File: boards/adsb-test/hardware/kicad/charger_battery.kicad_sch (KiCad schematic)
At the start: 0 parts

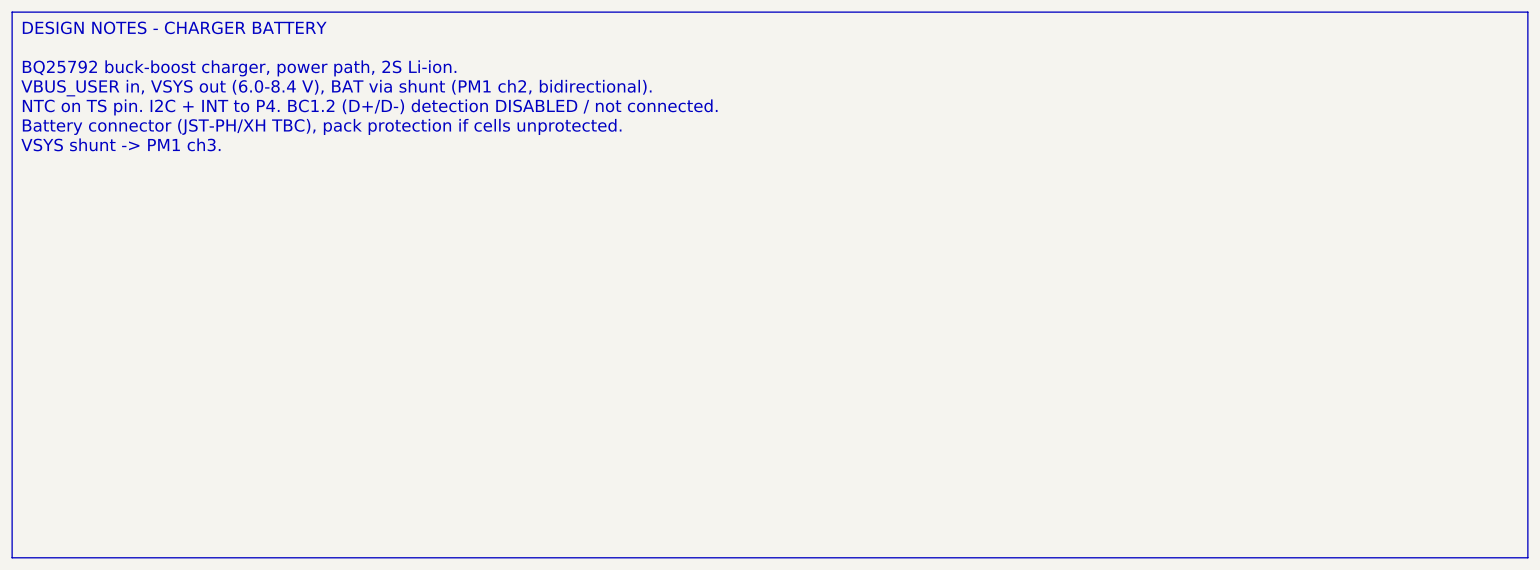
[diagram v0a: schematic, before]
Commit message: Release v0.4.0: ADSB_Test with ESP32-C5, ADSBee m1421 and LA5016 header
- C6 -> C5 co-processor; m1421 identified and integrated (symbol/footprint
  from the ADSBee 1421 carrier, GPL-3.0 attribution)
- Power budget and 2S1P battery sizing for >= 1 h; USB-A for 1-2 SDRs via hub
- Dev port: FT2232H + RP2040 debugprobe; TCA6408A expander for slow I/O
- Test Debug sheet with LA5016 header and rail test points
- Vendor documents git-ignored (public repo)

Co-Authored-By: Claude Opus 5.5 <noreply@anthropic.com>
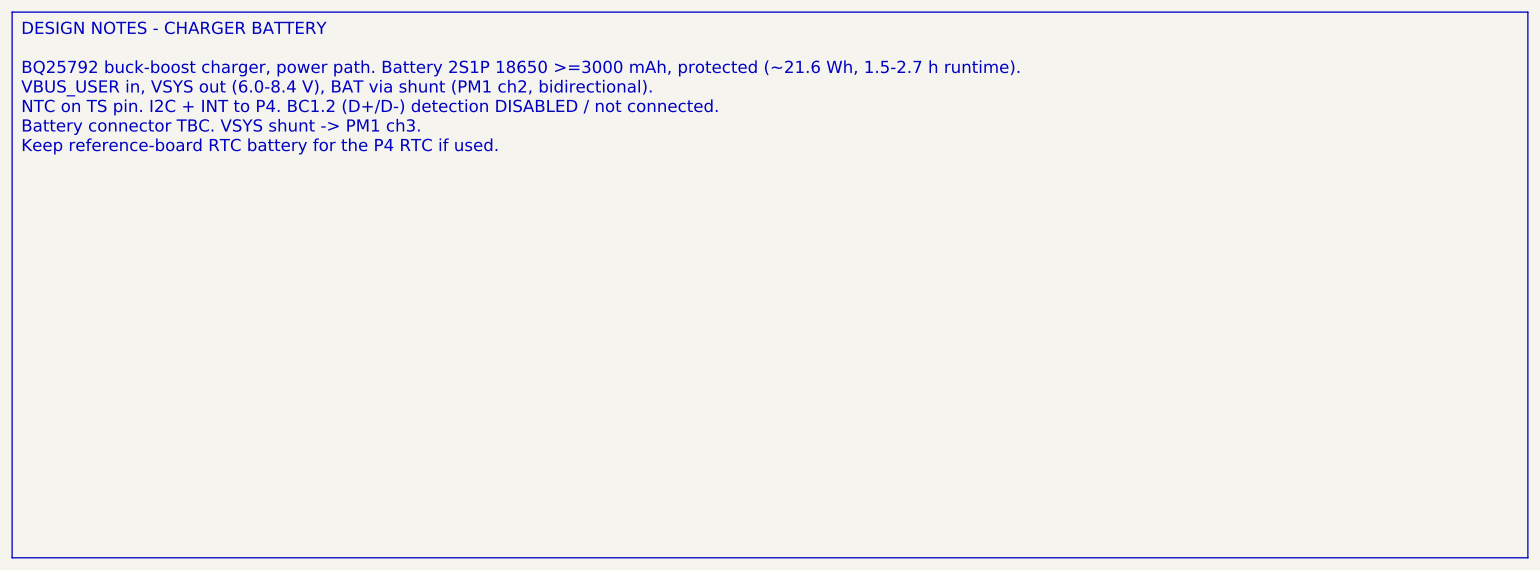
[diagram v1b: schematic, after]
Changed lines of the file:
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@@
 		(comment 1 "Requirements: boards/adsb-test/docs/requirements.md")
 	)
-	(text_box "DESIGN NOTES - CHARGER BATTERY\n\nBQ25792 buck-boost charger, power path, 2S Li-ion.\nVBUS_USER in, VSYS out (6.0-8.4 V), BAT via shunt (PM1 ch2, bidirectional).\nNTC on TS pin. I2C + INT to P4. BC1.2 (D+/D-) detection DISABLED / not connected.\nBattery connector (JST-PH/XH TBC), pack protection if cells unprotected.\nVSYS shunt -> PM1 ch3."
+	(text_box "DESIGN NOTES - CHARGER BATTERY\n\nBQ25792 buck-boost charger, power path. Battery 2S1P 18650 >=3000 mAh, protected (~21.6 Wh, 1.5-2.7 h runtime).\nVBUS_USER in, VSYS out (6.0-8.4 V), BAT via shunt (PM1 ch2, bidirectional).\nNTC on TS pin. I2C + INT to P4. BC1.2 (D+/D-) detection DISABLED / not connected.\nBattery connector TBC. VSYS shunt -> PM1 ch3.\nKeep reference-board RTC battery for the P4 RTC if used."
 		(exclude_from_sim no)
 		(at 20 20 0)
